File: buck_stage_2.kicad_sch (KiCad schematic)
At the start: 16 parts, among them U201 RT6365

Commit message: v2.0.0
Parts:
- C204, C205: LCSC C2918513 -> C77101
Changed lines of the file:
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@@
   (title_block
     (title "Sailor Hat for Raspberry Pi")
-    (date "2023-01-28")
-    (rev "v2.0.0-a4")
+    (date "2023-02-12")
+    (rev "v2.0.0")
     (company "Hat Labs Ltd")
     (comment 1 "https://creativecommons.org/licenses/by/4.0")
@@
       (effects (font (size 1.27 1.27)) hide)
     )
-    (property "LCSC" "C2918513" (id 5) (at 179.07 139.7 0)
+    (property "LCSC" "C77101" (id 5) (at 179.07 139.7 0)
       (effects (font (size 1.27 1.27)) hide)
     )
@@
       (effects (font (size 1.27 1.27)) hide)
     )
-    (property "LCSC" "C2918513" (id 5) (at 168.91 135.89 0)
-      (effects (font (size 1.27 1.27)) hide)
-    )
+    (property "LCSC" "C77101" (id 5) (at 168.91 135.89 0)
+      (effects (font (size 1.27 1.27)) hide)
+    )

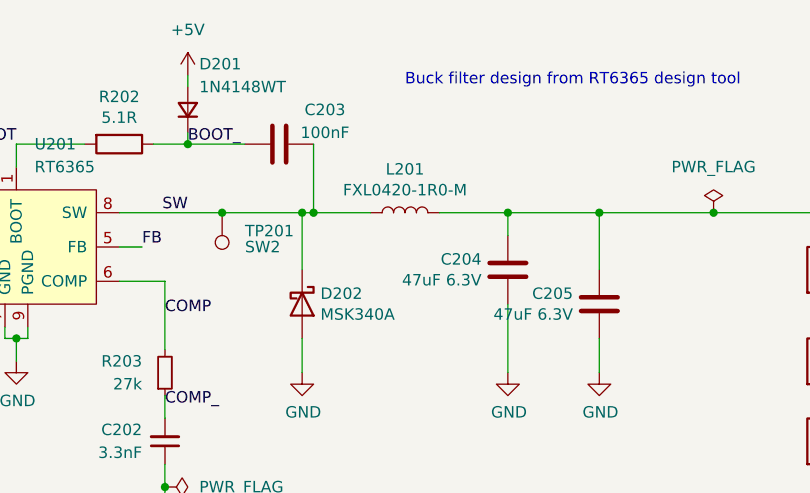
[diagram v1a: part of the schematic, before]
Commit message: Update C312 and R306
These changes fix the too high startup voltage and the first stage
buck converter stability issues.
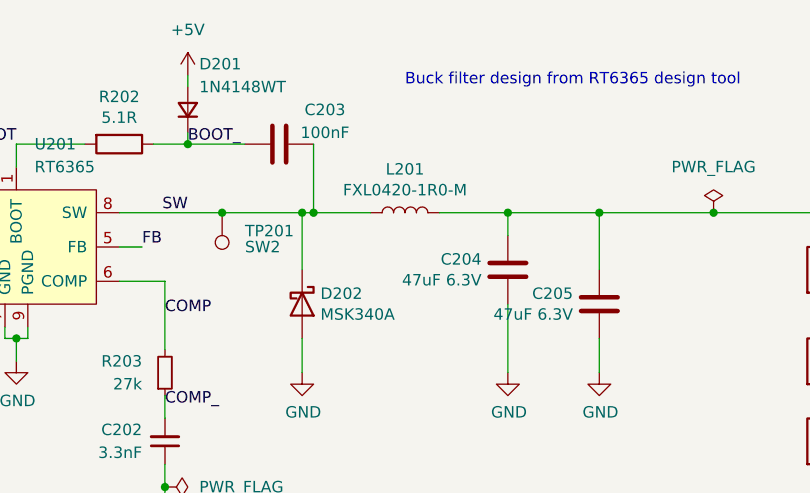
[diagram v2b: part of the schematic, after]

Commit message: Move rotation definitions to component fields
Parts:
- U201: JLCPCB_CORRECTION (none) -> 0;0;270
